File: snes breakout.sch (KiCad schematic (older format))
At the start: 5 parts

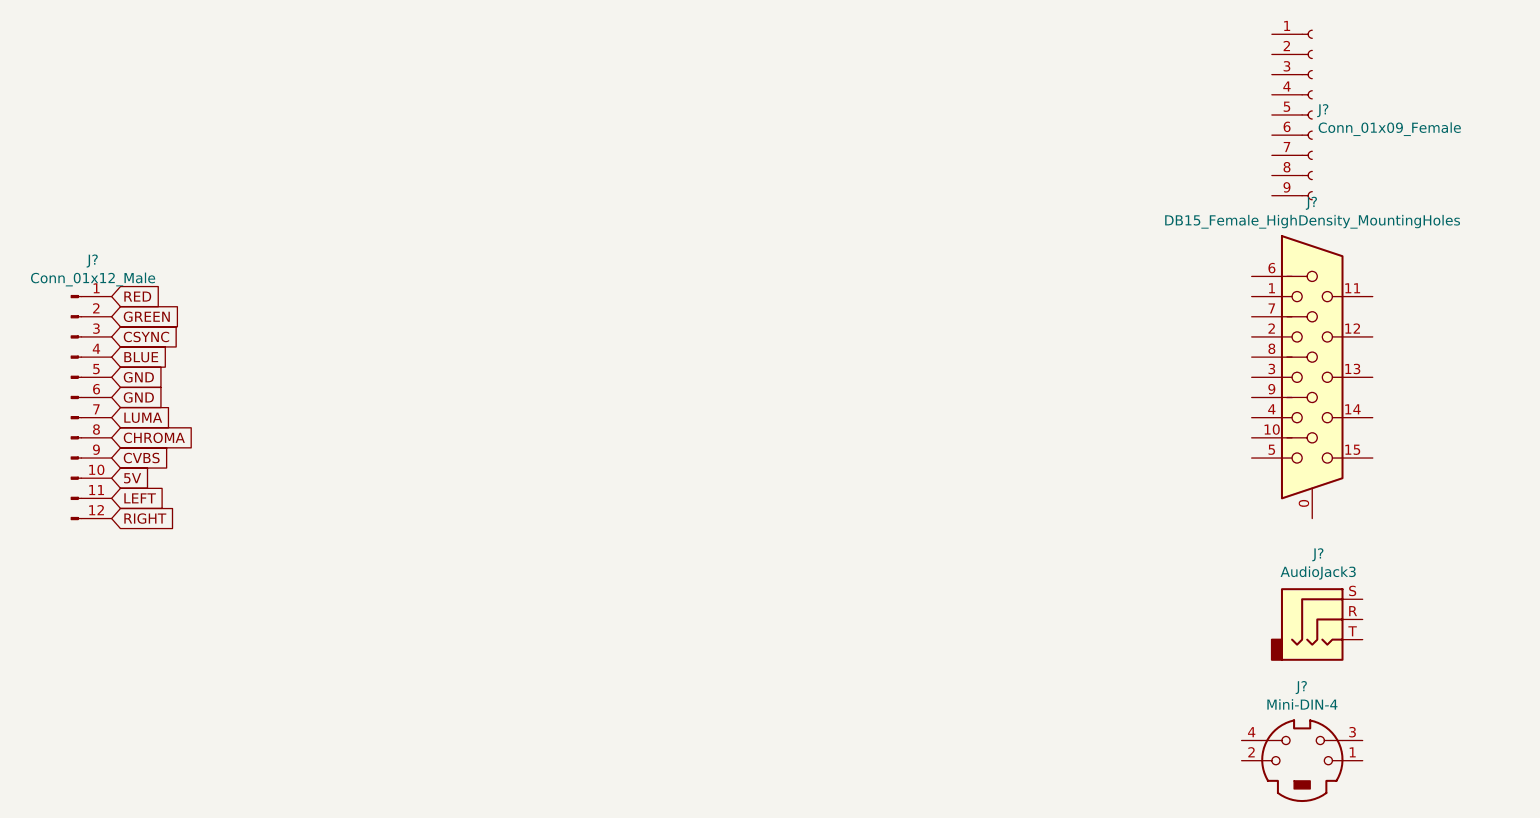
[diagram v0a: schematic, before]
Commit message: finished schematic, started board layout
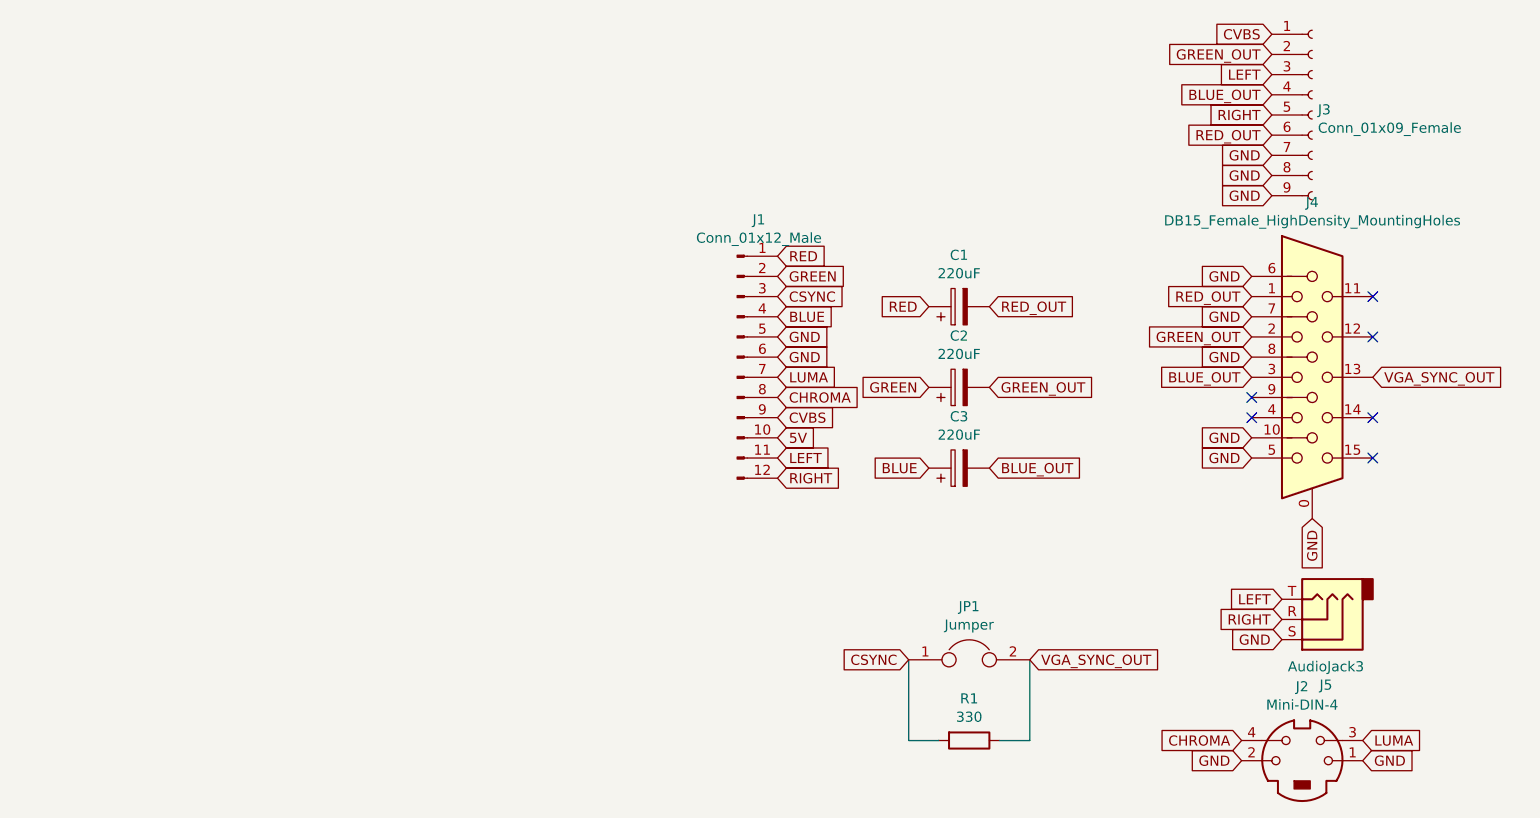
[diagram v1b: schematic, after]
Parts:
- added C1, C2, C3: 220uF, Capacitor_SMD:CP_Elec_6.3x5.4, symbol Device:CP
- added JP1: Jumper, Jumper:SolderJumper-2_P1.3mm_Open_TrianglePad1.0x1.5mm, symbol Device:Jumper
- added R1: 330, Resistor_SMD:R_0805_2012Metric_Pad1.15x1.40mm_HandSolder, symbol Device:R
- J1: renamed from J?; footprint (none) -> Tinkerplunk:SNES_PLUG
- J2: renamed from J?; footprint (none) -> Tinkerplunk:CUI_MD-40SG
- J3: renamed from J?; footprint (none) -> Tinkerplunk:3x2_RCA
- J4: renamed from J?; footprint (none) -> Tinkerplunk:VGA
- J5: renamed from J?; footprint (none) -> Tinkerplunk:CUI_SJ1-3533NG
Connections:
- net BLUE: now also C3.1
- net CHROMA: now also J2.4
- net CSYNC: now also JP1.1, R1.2
- net CVBS: now also J3.1 (Pin_1)
- net GND: now also J2.1, J2.2, J3.7 (Pin_7), J3.8 (Pin_8), J3.9 (Pin_9), J4.0, J4.10, J4.5, J4.6, J4.7, J4.8, J5.S
- net GREEN: now also C2.1
- net LEFT: now also J3.3 (Pin_3), J5.T
- net LUMA: now also J2.3
- net RED: now also C1.1
- net RIGHT: now also J3.5 (Pin_5), J5.R
- net GREEN_OUT: now reaches J3.2 (Pin_2)
- net GREEN_OUT: now also J4.2, C2.2
- net BLUE_OUT: now reaches J3.4 (Pin_4)
- net BLUE_OUT: now also J4.3, C3.2
- net RED_OUT: now reaches J3.6 (Pin_6)
- net RED_OUT: now also J4.1, C1.2
- net VGA_SYNC_OUT: now reaches J4.13
- net VGA_SYNC_OUT: now also JP1.2, R1.1
- no-connect marks 0 -> 6
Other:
- moved on the sheet: J1, J5
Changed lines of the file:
@@
 EESchema Schematic File Version 4
+LIBS:snes breakout-cache
 EELAYER 29 0
 EELAYER END
@@
 $EndDescr
 $Comp
-L Connector:Conn_01x12_Male J?
+L Connector:Conn_01x12_Male J1
 U 1 1 5D1A4161
-P 1650 3250
-F 0 "J?" H 1758 3931 50  0000 C CNN
-F 1 "Conn_01x12_Male" H 1758 3840 50  0000 C CNN
-F 2 "" H 1650 3250 50  0001 C CNN
-F 3 "~" H 1650 3250 50  0001 C CNN
-	1    1650 3250
-	1    0    0    -1
-$EndComp
-$Comp
-L Connector:Conn_01x09_Female J?
+P 4950 3050
+F 0 "J1" H 5058 3731 50  0000 C CNN
+F 1 "Conn_01x12_Male" H 5058 3640 50  0000 C CNN
+F 2 "Tinkerplunk:SNES_PLUG" H 4950 3050 50  0001 C CNN
+F 3 "~" H 4950 3050 50  0001 C CNN
+	1    4950 3050
+	1    0    0    -1
+$EndComp
+$Comp
+L Connector:Conn_01x09_Female J3
 U 1 1 5D1A4EE0
 P 7800 1850
-F 0 "J?" H 7828 1876 50  0000 L CNN
+F 0 "J3" H 7828 1876 50  0000 L CNN
 F 1 "Conn_01x09_Female" H 7828 1785 50  0000 L CNN
-F 2 "" H 7800 1850 50  0001 C CNN
+F 2 "Tinkerplunk:3x2_RCA" H 7800 1850 50  0001 C CNN
 F 3 "~" H 7800 1850 50  0001 C CNN
 	1    7800 1850
@@
 $EndComp
 $Comp
-L Connector:DB15_Female_HighDensity_MountingHoles J?
+L Connector:DB15_Female_HighDensity_MountingHoles J4
 U 1 1 5D1A5ADF
 P 7800 3150
-F 0 "J?" H 7800 4017 50  0000 C CNN
+F 0 "J4" H 7800 4017 50  0000 C CNN
 F 1 "DB15_Female_HighDensity_MountingHoles" H 7800 3926 50  0000 C CNN
-F 2 "" H 6850 3550 50  0001 C CNN
+F 2 "Tinkerplunk:VGA" H 6850 3550 50  0001 C CNN
 F 3 " ~" H 6850 3550 50  0001 C CNN
 	1    7800 3150
@@
 $EndComp
 $Comp
-L Connector:Mini-DIN-4 J?
+L Connector:Mini-DIN-4 J2
 U 1 1 5D1A7DD6
 P 7750 5050
-F 0 "J?" H 7750 5417 50  0000 C CNN
+F 0 "J2" H 7750 5417 50  0000 C CNN
 F 1 "Mini-DIN-4" H 7750 5326 50  0000 C CNN
-F 2 "" H 7750 5050 50  0001 C CNN
+F 2 "Tinkerplunk:CUI_MD-40SG" H 7750 5050 50  0001 C CNN
 F 3 "http://service.powerdynamics.com/ec/Catalog17/Section%2011.pdf" H 7750 5050 50  0001 C CNN
 	1    7750 5050
@@
 $EndComp
 $Comp
-L Connector:AudioJack3 J?
+L Connector:AudioJack3 J5
 U 1 1 5D1A86E1
 P 7850 4350
-F 0 "J?" H 7832 4675 50  0000 C CNN
+F 0 "J5" H 7832 4675 50  0000 C CNN
 F 1 "AudioJack3" H 7832 4584 50  0000 C CNN
-F 2 "" H 7850 4350 50  0001 C CNN
+F 2 "Tinkerplunk:CUI_SJ1-3533NG" H 7850 4350 50  0001 C CNN
 F 3 "~" H 7850 4350 50  0001 C CNN
 	1    7850 4350
-	1    0    0    -1
-$EndComp
-Text GLabel 1850 2750 2    50   Input ~ 0
+	-1   0    0    1
+$EndComp
+Text GLabel 5150 2550 2    50   Input ~ 0
 RED
-Text GLabel 1850 2850 2    50   Input ~ 0
+Text GLabel 5150 2650 2    50   Input ~ 0
 GREEN
-Text GLabel 1850 2950 2    50   Input ~ 0
+Text GLabel 5150 2750 2    50   Input ~ 0
 CSYNC
-Text GLabel 1850 3050 2    50   Input ~ 0
+Text GLabel 5150 2850 2    50   Input ~ 0
 BLUE
-Text GLabel 1850 3150 2    50   Input ~ 0
-GND
-Text GLabel 1850 3250 2    50   Input ~ 0
-GND
-Text GLabel 1850 3350 2    50   Input ~ 0
+Text GLabel 5150 2950 2    50   Input ~ 0
+GND
+Text GLabel 5150 3050 2    50   Input ~ 0
+GND
+Text GLabel 5150 3150 2    50   Input ~ 0
 LUMA
-Text GLabel 1850 3450 2    50   Input ~ 0
+Text GLabel 5150 3250 2    50   Input ~ 0
 CHROMA
-Text GLabel 1850 3550 2    50   Input ~ 0
+Text GLabel 5150 3350 2    50   Input ~ 0
 CVBS
-Text GLabel 1850 3650 2    50   Input ~ 0
+Text GLabel 5150 3450 2    50   Input ~ 0
 5V
-Text GLabel 1850 3750 2    50   Input ~ 0
+Text GLabel 5150 3550 2    50   Input ~ 0
 LEFT
-Text GLabel 1850 3850 2    50   Input ~ 0
+Text GLabel 5150 3650 2    50   Input ~ 0
 RIGHT
+$Comp
+L Device:CP C1
+U 1 1 5D1B9384
+P 6050 2800
+F 0 "C1" V 6305 2800 50  0000 C CNN
+F 1 "220uF" V 6214 2800 50  0000 C CNN
+F 2 "Capacitor_SMD:CP_Elec_6.3x5.4" H 6088 2650 50  0001 C CNN
+F 3 "~" H 6050 2800 50  0001 C CNN
+	1    6050 2800
+	0    -1   -1   0
+$EndComp
+$Comp
+L Device:CP C2
+U 1 1 5D1BD373
+P 6050 3200
+F 0 "C2" V 6305 3200 50  0000 C CNN
+F 1 "220uF" V 6214 3200 50  0000 C CNN
+F 2 "Capacitor_SMD:CP_Elec_6.3x5.4" H 6088 3050 50  0001 C CNN
+F 3 "~" H 6050 3200 50  0001 C CNN
+	1    6050 3200
+	0    -1   -1   0
+$EndComp
+$Comp
+L Device:CP C3
+U 1 1 5D1BD94B
+P 6050 3600
+F 0 "C3" V 6305 3600 50  0000 C CNN
+F 1 "220uF" V 6214 3600 50  0000 C CNN
+F 2 "Capacitor_SMD:CP_Elec_6.3x5.4" H 6088 3450 50  0001 C CNN
+F 3 "~" H 6050 3600 50  0001 C CNN
+	1    6050 3600
+	0    -1   -1   0
+$EndComp
+Text GLabel 5900 2800 0    50   Input ~ 0
+RED
+Text GLabel 5900 3200 0    50   Input ~ 0
+GREEN
+Text GLabel 5900 3600 0    50   Input ~ 0
+BLUE
+Text GLabel 6200 2800 2    50   Input ~ 0
+RED_OUT
+Text GLabel 6200 3200 2    50   Input ~ 0
+GREEN_OUT
+Text GLabel 6200 3600 2    50   Input ~ 0
+BLUE_OUT
+Text GLabel 7500 2750 0    50   Input ~ 0
+RED_OUT
+Text GLabel 7500 2650 0    50   Input ~ 0
+GND
+Text GLabel 7500 2850 0    50   Input ~ 0
+GND
+Text GLabel 7500 2950 0    50   Input ~ 0
+GREEN_OUT
+Text GLabel 7500 3050 0    50   Input ~ 0
+GND
+Text GLabel 7500 3150 0    50   Input ~ 0
+BLUE_OUT
+Text GLabel 7500 3450 0    50   Input ~ 0
+GND
+Text GLabel 7500 3550 0    50   Input ~ 0
+GND
+Text GLabel 8100 3150 2    50   Input ~ 0
+VGA_SYNC_OUT
+Text GLabel 7800 3850 3    50   Input ~ 0
+GND
+NoConn ~ 8100 2750
+NoConn ~ 8100 2950
+NoConn ~ 8100 3350
+NoConn ~ 8100 3550
+NoConn ~ 7500 3350
+NoConn ~ 7500 3250
+Text GLabel 8050 4950 2    50   Input ~ 0
+LUMA
+Text GLabel 7450 4950 0    50   Input ~ 0
+CHROMA
+Text GLabel 7450 5050 0    50   Input ~ 0
+GND
+Text GLabel 8050 5050 2    50   Input ~ 0
+GND
+Text GLabel 7650 4250 0    50   Input ~ 0
+LEFT
+Text GLabel 7650 4350 0    50   Input ~ 0
+RIGHT
+Text GLabel 7650 4450 0    50   Input ~ 0
+GND
+Text GLabel 7600 1450 0    50   Input ~ 0
+CVBS
+Text GLabel 7600 1550 0    50   Input ~ 0
+GREEN_OUT
+Text GLabel 7600 1650 0    50   Input ~ 0
+LEFT
+Text GLabel 7600 1750 0    50   Input ~ 0
+BLUE_OUT
+Text GLabel 7600 1850 0    50   Input ~ 0
+RIGHT
+Text GLabel 7600 1950 0    50   Input ~ 0
+RED_OUT
+Text GLabel 7600 2050 0    50   Input ~ 0
+GND
+Text GLabel 7600 2150 0    50   Input ~ 0
+GND
+Text GLabel 7600 2250 0    50   Input ~ 0
+GND
+$Comp
+L Device:R R1
+U 1 1 5D1C3F5A
+P 6100 4950
+F 0 "R1" V 5893 4950 50  0000 C CNN
+F 1 "330" V 5984 4950 50  0000 C CNN
+F 2 "Resistor_SMD:R_0805_2012Metric_Pad1.15x1.40mm_HandSolder" V 6030 4950 50  0001 C CNN
+F 3 "~" H 6100 4950 50  0001 C CNN
+	1    6100 4950
+	0    1    1    0
+$EndComp
+$Comp
+L Device:Jumper JP1
+U 1 1 5D1C47B0
+P 6100 4550
+F 0 "JP1" H 6100 4814 50  0000 C CNN
+F 1 "Jumper" H 6100 4723 50  0000 C CNN
+F 2 "Jumper:SolderJumper-2_P1.3mm_Open_TrianglePad1.0x1.5mm" H 6100 4550 50  0001 C CNN
+F 3 "~" H 6100 4550 50  0001 C CNN
+	1    6100 4550
+	1    0    0    -1
+$EndComp
+Text GLabel 5800 4550 0    50   Input ~ 0
+CSYNC
+Text GLabel 6400 4550 2    50   Input ~ 0
+VGA_SYNC_OUT
+Wire Wire Line
+	5950 4950 5800 4950
+Wire Wire Line
+	5800 4950 5800 4550
+Wire Wire Line
+	6250 4950 6400 4950
+Wire Wire Line
+	6400 4950 6400 4550
 $EndSCHEMATC

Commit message: Generated gerbers
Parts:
- R1: footprint Resistor_SMD:R_0805_2012Metric_Pad1.15x1.40mm_HandSolder -> Resistor_SMD:R_0603_1608Metric_Pad1.05x0.95mm_HandSolder
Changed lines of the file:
@@
 F 0 "R1" V 5893 4950 50  0000 C CNN
 F 1 "330" V 5984 4950 50  0000 C CNN
-F 2 "Resistor_SMD:R_0805_2012Metric_Pad1.15x1.40mm_HandSolder" V 6030 4950 50  0001 C CNN
+F 2 "Resistor_SMD:R_0603_1608Metric_Pad1.05x0.95mm_HandSolder" V 6030 4950 50  0001 C CNN
 F 3 "~" H 6100 4950 50  0001 C CNN
 	1    6100 4950
